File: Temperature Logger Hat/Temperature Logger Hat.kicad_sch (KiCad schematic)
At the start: 18 parts, among them J1 GPIO, J2 SPI, J3 1-wire, J4 Jumper_Mode, SW1 SW_Power_Off, SW2 SW_Mode2, U1 CAT24C256

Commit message: Update schematic
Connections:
- net GPIO6: now also SW2.1 (A)
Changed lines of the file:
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@@
 	(wire
 		(pts
-			(xy 120.65 97.79) (xy 119.38 97.79)
+			(xy 119.38 99.06) (xy 149.86 99.06)
 		)
 		(stroke
@@
 	(wire
 		(pts
-			(xy 120.65 99.06) (xy 149.86 99.06)
-		)
-		(stroke
-			(width 0)
-			(type solid)
-		)
-	)
-	(wire
-		(pts
 			(xy 165.1 63.5) (xy 162.56 63.5)
 		)
@@
 	(wire
 		(pts
-			(xy 119.38 97.79) (xy 119.38 118.11)
-		)
-		(stroke
+			(xy 119.38 99.06) (xy 119.38 118.11)
+		)
+		(stroke

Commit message: Update documentation
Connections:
- net GPIO9/SPI0.MISO: no longer J2.3 (Pin_3)
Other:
- note added: "CS"
- note added: "SCK"
- note added: "SDI"
- note added: "SDO"
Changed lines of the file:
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@@
+		)
+	)
+	(text "SDO"
+		(exclude_from_sim no)
+		(at 65.786 100.838 0)
+		(effects
+			(font
+				(size 1.27 1.27)
+			)
 		)
 	)
@@
 		)
 	)
+	(text "SDI\n"
+		(exclude_from_sim no)
+		(at 65.532 98.298 0)
+		(effects
+			(font
+				(size 1.27 1.27)
+			)
+		)
+	)
+	(text "SCK"
+		(exclude_from_sim no)
+		(at 65.532 103.378 0)
+		(effects
+			(font
+				(size 1.27 1.27)
+			)
+		)
+	)
+	(text "CS"
+		(exclude_from_sim no)
+		(at 65.278 95.504 0)
+		(effects
+			(font
+				(size 1.27 1.27)
+			)
+		)
+	)
 	(junction
 		(at 165.1 41.91)
@@
 	(junction
 		(at 200.66 41.91)
-		(diameter 0)
-		(color 0 0 0 0)
-	)
-	(junction
-		(at 67.31 101.6)
 		(diameter 0)
 		(color 0 0 0 0)
@@
 	(wire
 		(pts
-			(xy 68.58 101.6) (xy 67.31 101.6)
-		)
-		(stroke
-			(width 0)
-			(type default)
-		)
-	)
-	(wire
-		(pts
 			(xy 165.1 76.2) (xy 165.1 83.82)
 		)
@@
 	(wire
 		(pts
+			(xy 55.88 101.6) (xy 68.58 101.6)
+		)
+		(stroke
+			(width 0)
+			(type default)
+		)
+	)
+	(wire
+		(pts
 			(xy 162.56 99.06) (xy 189.23 99.06)
 		)
@@
 		)
 		(stroke
-			(width 0)
-			(type default)
-		)
-	)
-	(wire
-		(pts
-			(xy 67.31 101.6) (xy 55.88 101.6)
-		)
-		(stroke

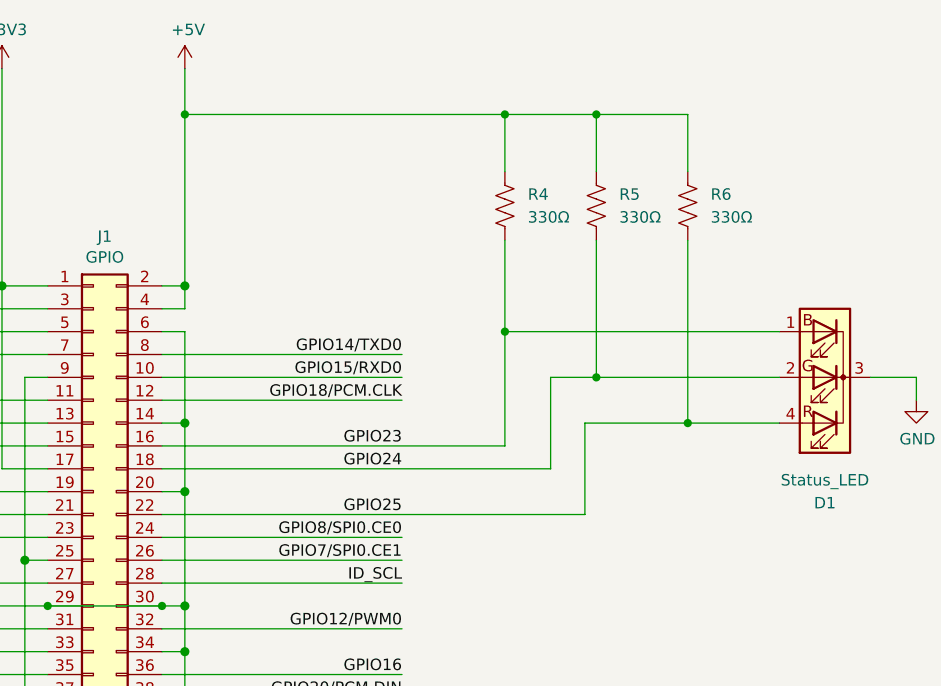
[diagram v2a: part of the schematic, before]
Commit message: Fix LED connections in schematic
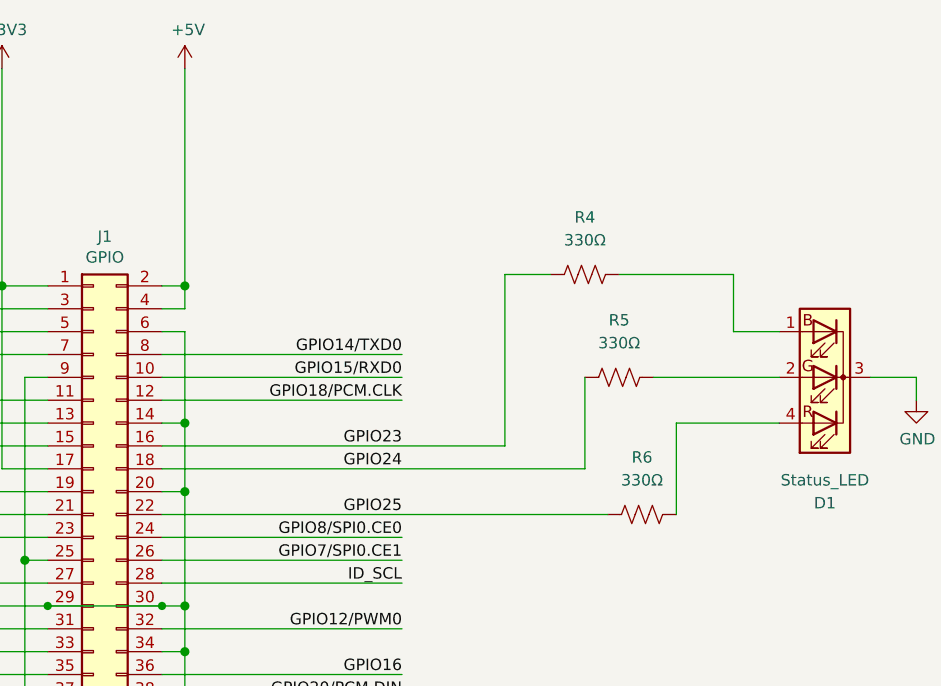
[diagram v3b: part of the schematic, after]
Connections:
- net +5V: no longer R4.1, R5.1, R6.1
- net GPIO23: no longer D1.1 (BA)
- net GPIO24: no longer D1.2 (GA)
- net GPIO25: no longer D1.4 (RA)
- new net: D1.4 (RA), R6.1
- new net: D1.1 (BA), R4.1
- new net: D1.2 (GA), R5.1
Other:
- moved on the sheet: R4, R5, R6
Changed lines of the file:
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@@
 	)
 	(junction
-		(at 165.1 41.91)
-		(diameter 0)
-		(color 0 0 0 0)
-	)
-	(junction
 		(at 93.98 175.26)
 		(diameter 1.016)
@@
 	)
 	(junction
-		(at 200.66 66.04)
-		(diameter 0)
-		(color 0 0 0 0)
-	)
-	(junction
 		(at 147.32 109.22)
 		(diameter 1.016)
@@
 	)
 	(junction
-		(at 220.98 76.2)
-		(diameter 0)
-		(color 0 0 0 0)
-	)
-	(junction
 		(at 165.1 101.6)
 		(diameter 1.016)
@@
 	)
 	(junction
-		(at 200.66 41.91)
-		(diameter 0)
-		(color 0 0 0 0)
-	)
-	(junction
 		(at 165.1 96.52)
 		(diameter 1.016)
@@
 	)
 	(junction
-		(at 210.82 71.12)
-		(diameter 0)
-		(color 0 0 0 0)
-	)
-	(junction
 		(at 80.01 68.58)
 		(diameter 0)
@@
 	)
 	(junction
-		(at 210.82 41.91)
-		(diameter 0)
-		(color 0 0 0 0)
-	)
-	(junction
 		(at 144.78 60.96)
 		(diameter 1.016)
@@
 	(wire
 		(pts
-			(xy 220.98 48.26) (xy 220.98 41.91)
-		)
-		(stroke
-			(width 0)
-			(type default)
-		)
-	)
-	(wire
-		(pts
 			(xy 80.01 68.58) (xy 73.66 68.58)
 		)
@@
 	(wire
 		(pts
+			(xy 200.66 78.74) (xy 200.66 59.69)
+		)
+		(stroke
+			(width 0)
+			(type solid)
+		)
+	)
+	(wire
+		(pts
 			(xy 91.44 175.26) (xy 93.98 175.26)
 		)
@@
 	(wire
 		(pts
-			(xy 205.74 71.12) (xy 205.74 81.28)
+			(xy 209.55 71.12) (xy 209.55 81.28)
 		)
 		(stroke
@@
 	(wire
 		(pts
-			(xy 209.55 76.2) (xy 209.55 86.36)
-		)
-		(stroke
-			(width 0)
-			(type default)
-		)
-	)
-	(wire
-		(pts
-			(xy 220.98 76.2) (xy 209.55 76.2)
+			(xy 226.06 59.69) (xy 226.06 66.04)
 		)
 		(stroke
@@
 	(wire
 		(pts
-			(xy 200.66 66.04) (xy 200.66 78.74)
+			(xy 219.71 76.2) (xy 231.14 76.2)
 		)
 		(stroke
@@
 	(wire
 		(pts
-			(xy 231.14 66.04) (xy 200.66 66.04)
-		)
-		(stroke
-			(width 0)
-			(type default)
-		)
-	)
-	(wire
-		(pts
 			(xy 67.31 104.14) (xy 53.34 104.14)
 		)
@@
 	(wire
 		(pts
-			(xy 91.44 104.14) (xy 91.44 120.65)
+			(xy 219.71 86.36) (xy 219.71 76.2)
 		)
 		(stroke
@@
 	(wire
 		(pts
-			(xy 200.66 55.88) (xy 200.66 66.04)
+			(xy 91.44 104.14) (xy 91.44 120.65)
 		)
 		(stroke
@@
 	(wire
 		(pts
-			(xy 200.66 48.26) (xy 200.66 41.91)
-		)
-		(stroke
-			(width 0)
-			(type default)
-		)
-	)
-	(wire
-		(pts
 			(xy 149.86 63.5) (xy 120.65 63.5)
 		)
@@
 	(wire
 		(pts
-			(xy 210.82 41.91) (xy 210.82 48.26)
+			(xy 165.1 60.96) (xy 165.1 63.5)
 		)
 		(stroke
 			(width 0)
-			(type default)
+			(type solid)
 		)
 	)
 	(wire
 		(pts
-			(xy 165.1 60.96) (xy 165.1 63.5)
+			(xy 200.66 59.69) (xy 205.74 59.69)
 		)
 		(stroke
@@
 	(wire
 		(pts
-			(xy 165.1 36.83) (xy 165.1 41.91)
+			(xy 165.1 36.83) (xy 165.1 60.96)
 		)
 		(stroke
@@
 	(wire
 		(pts
-			(xy 210.82 71.12) (xy 205.74 71.12)
-		)
-		(stroke
-			(width 0)
-			(type default)
-		)
-	)
-	(wire
-		(pts
 			(xy 93.98 165.1) (xy 93.98 167.64)
 		)
@@
 	(wire
 		(pts
-			(xy 162.56 81.28) (xy 205.74 81.28)
+			(xy 162.56 81.28) (xy 209.55 81.28)
 		)
 		(stroke
@@
 	(wire
 		(pts
+			(xy 217.17 71.12) (xy 231.14 71.12)
+		)
+		(stroke
+			(width 0)
+			(type default)
+		)
+	)
+	(wire
+		(pts
 			(xy 246.38 71.12) (xy 246.38 73.66)
 		)
@@
 	(wire
 		(pts
-			(xy 210.82 41.91) (xy 220.98 41.91)
-		)
-		(stroke
-			(width 0)
-			(type default)
-		)
-	)
-	(wire
-		(pts
 			(xy 55.88 101.6) (xy 68.58 101.6)
 		)
@@
 	(wire
 		(pts
-			(xy 165.1 41.91) (xy 200.66 41.91)
-		)
-		(stroke
-			(width 0)
-			(type default)
-		)
-	)
-	(wire
-		(pts
-			(xy 200.66 41.91) (xy 210.82 41.91)
-		)
-		(stroke
-			(width 0)
-			(type default)
-		)
-	)
-	(wire
-		(pts
 			(xy 162.56 106.68) (xy 189.23 106.68)
 		)
@@
 	(wire
 		(pts
-			(xy 210.82 55.88) (xy 210.82 71.12)
+			(xy 226.06 66.04) (xy 231.14 66.04)
 		)
 		(stroke
@@
 	(wire
 		(pts
-			(xy 162.56 86.36) (xy 209.55 86.36)
+			(xy 162.56 86.36) (xy 212.09 86.36)
 		)
 		(stroke
@@
 	(wire
 		(pts
-			(xy 165.1 41.91) (xy 165.1 60.96)
-		)
-		(stroke
-			(width 0)
-			(type solid)
-		)
-	)
-	(wire
-		(pts
-			(xy 231.14 71.12) (xy 210.82 71.12)
-		)
-		(stroke
-			(width 0)
-			(type default)
-		)
-	)
-	(wire
-		(pts
-			(xy 231.14 76.2) (xy 220.98 76.2)
+			(xy 91.44 120.65) (xy 102.87 120.65)
 		)
 		(stroke
@@
 	(wire
 		(pts
-			(xy 220.98 55.88) (xy 220.98 76.2)
+			(xy 162.56 93.98) (xy 189.23 93.98)
 		)
 		(stroke
 			(width 0)
-			(type default)
+			(type solid)
 		)
 	)
 	(wire
 		(pts
-			(xy 91.44 120.65) (xy 102.87 120.65)
+			(xy 213.36 59.69) (xy 226.06 59.69)
 		)
 		(stroke
@@
 	(wire
 		(pts
-			(xy 162.56 93.98) (xy 189.23 93.98)
-		)
-		(stroke
-			(width 0)
-			(type solid)
-		)
-	)
-	(wire
-		(pts
 			(xy 60.96 92.71) (xy 100.33 92.71)
 		)
@@
 	(symbol
 		(lib_id "Device:R_US")
-		(at 220.98 52.07 0)
+		(at 215.9 86.36 270)
 		(unit 1)
 		(exclude_from_sim no)
@@
 		(fields_autoplaced yes)
 		(property "Reference" "R6"
-			(at 223.52 50.7999 0)
+			(at 215.9 80.01 90)
 			(effects
 				(font
 					(size 1.27 1.27)
 				)
-				(justify left)
 			)
 		)
 		(property "Value" "330Ω"
-			(at 223.52 53.3399 0)
+			(at 215.9 82.55 90)
 			(effects
 				(font
 					(size 1.27 1.27)
 				)
-				(justify left)
 			)
 		)
 		(property "Footprint" ""
-			(at 221.996 52.324 90)
+			(at 215.646 87.376 90)
 			(effects
 				(font
@@
 		)
 		(property "Datasheet" "~"
-			(at 220.98 52.07 0)
+			(at 215.9 86.36 0)
 			(effects
 				(font
@@
 		)
 		(property "Description" "Resistor, US symbol"
-			(at 220.98 52.07 0)
+			(at 215.9 86.36 0)
 			(effects
 				(font
@@
 	(symbol
 		(lib_id "Device:R_US")
-		(at 200.66 52.07 0)
+		(at 209.55 59.69 270)
 		(unit 1)
 		(exclude_from_sim no)
@@
 		(fields_autoplaced yes)
 		(property "Reference" "R4"
-			(at 203.2 50.7999 0)
+			(at 209.55 53.34 90)
 			(effects
 				(font
 					(size 1.27 1.27)
 				)
-				(justify left)
 			)
 		)
 		(property "Value" "330Ω"
-			(at 203.2 53.3399 0)
+			(at 209.55 55.88 90)
 			(effects
 				(font
 					(size 1.27 1.27)
 				)
-				(justify left)
 			)
 		)
 		(property "Footprint" ""
-			(at 201.676 52.324 90)
+			(at 209.296 60.706 90)
 			(effects
 				(font
@@
 		)
 		(property "Datasheet" "~"
-			(at 200.66 52.07 0)
+			(at 209.55 59.69 0)
 			(effects
 				(font
@@
 		)
 		(property "Description" "Resistor, US symbol"
-			(at 200.66 52.07 0)
+			(at 209.55 59.69 0)
 			(effects
 				(font
@@
 	(symbol
 		(lib_id "Device:R_US")
-		(at 210.82 52.07 0)
+		(at 213.36 71.12 270)
 		(unit 1)
 		(exclude_from_sim no)
@@
 		(fields_autoplaced yes)
 		(property "Reference" "R5"
-			(at 213.36 50.7999 0)
+			(at 213.36 64.77 90)
 			(effects
 				(font
 					(size 1.27 1.27)
 				)
-				(justify left)
 			)
 		)
 		(property "Value" "330Ω"
-			(at 213.36 53.3399 0)
+			(at 213.36 67.31 90)
 			(effects
 				(font
 					(size 1.27 1.27)
 				)
-				(justify left)
 			)
 		)
 		(property "Footprint" ""
-			(at 211.836 52.324 90)
+			(at 213.106 72.136 90)
 			(effects
 				(font
@@
 		)
 		(property "Datasheet" "~"
-			(at 210.82 52.07 0)
+			(at 213.36 71.12 0)
 			(effects
 				(font
@@
 		)
 		(property "Description" "Resistor, US symbol"
-			(at 210.82 52.07 0)
+			(at 213.36 71.12 0)
 			(effects
 				(font
